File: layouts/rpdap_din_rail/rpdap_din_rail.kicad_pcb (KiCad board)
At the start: 2 copper layers, 95 x 50 mm, 67 parts

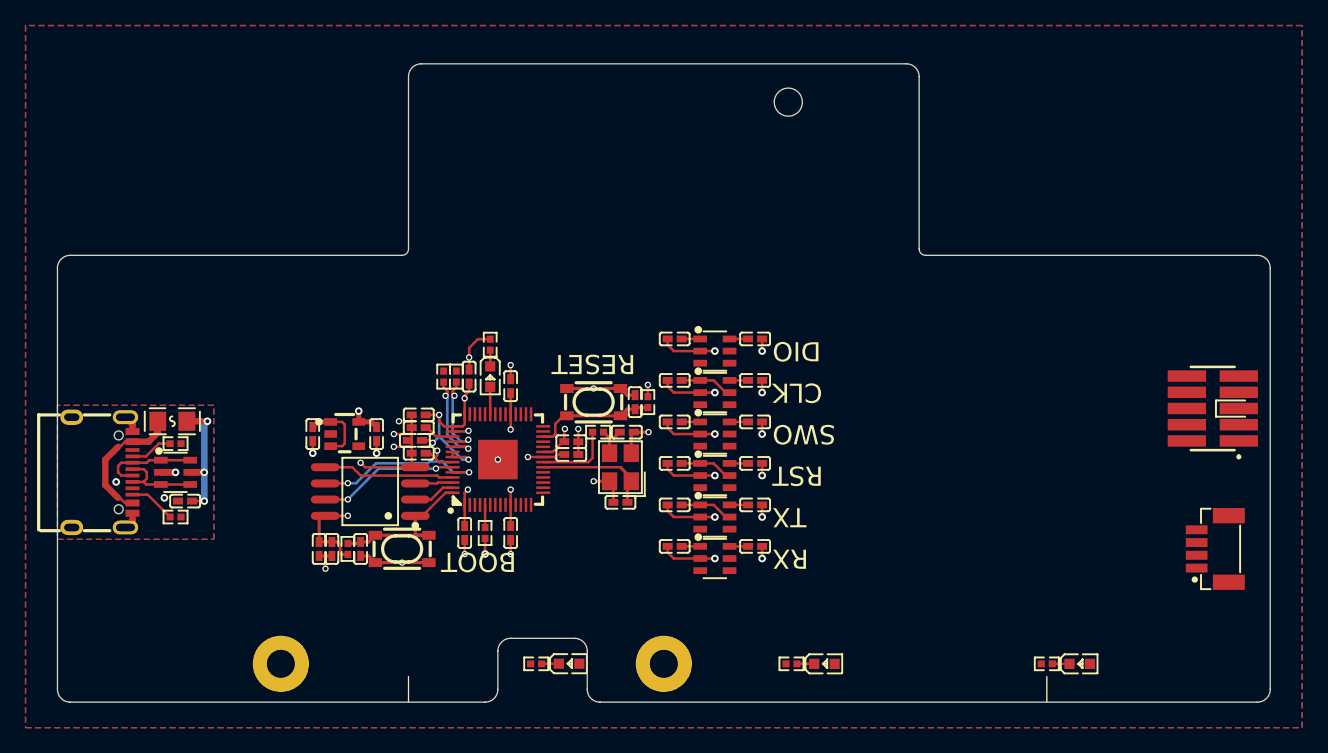
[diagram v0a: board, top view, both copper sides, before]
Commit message: update layouts and add jlink base compact layout
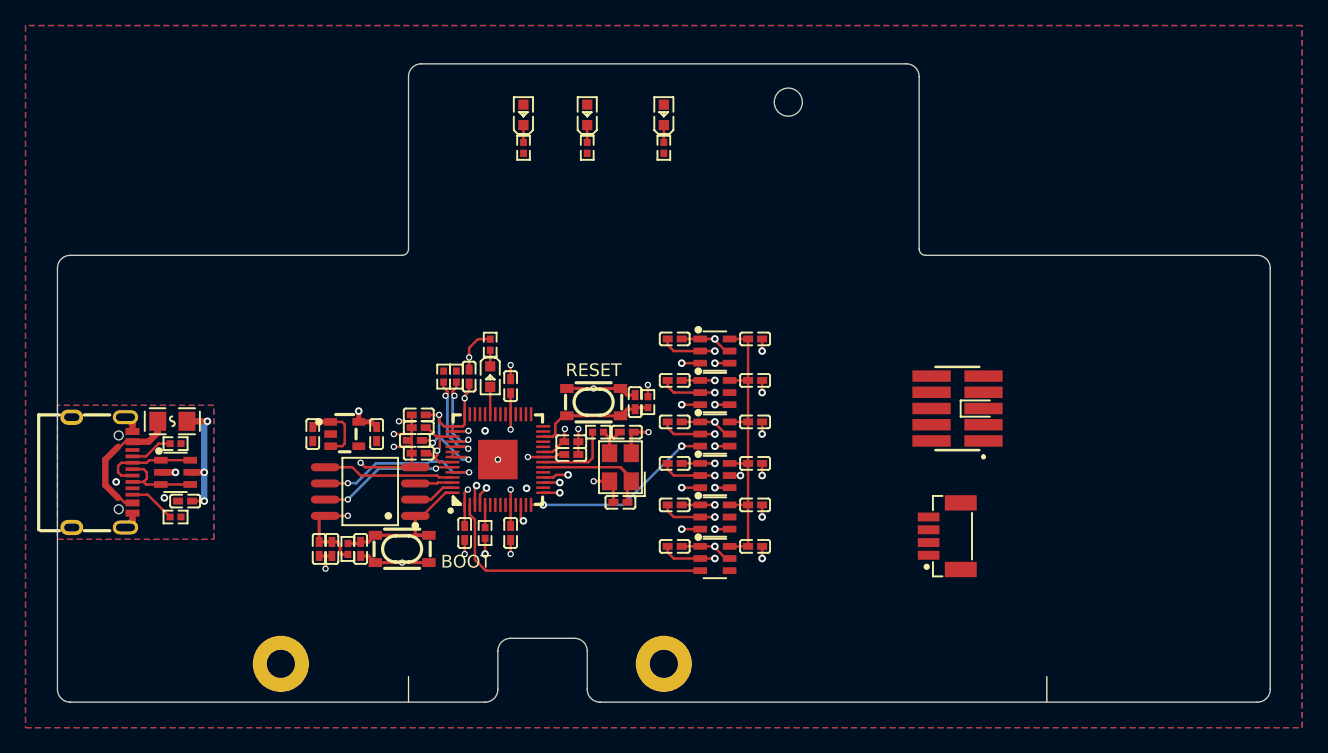
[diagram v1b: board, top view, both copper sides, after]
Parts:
- moved LED4 53.9 mm to (10.0, -43.0), turned to 90 degrees
- moved R12 50.3 mm to (10.0, -40.4), turned to -90 degrees
- moved LED3 46.8 mm to (4.00, -43.0), turned to 90 degrees
- moved R11 43.5 mm to (4.00, -40.4), turned to -90 degrees
- moved LED2 43.1 mm to (-1.00, -43.0), turned to 90 degrees
- moved R10 40.4 mm to (-0.99, -40.4), turned to -90 degrees
- moved U10 21.0 mm to (32.0, -10.0)
- moved CN1 20.0 mm to (33.0, -20.0)
- moved C10 9.75 mm to (17.2, -25.4)
- moved C3 9.75 mm to (10.8, -15.7)
- moved C4 9.75 mm to (17.2, -15.7)
- moved C9 9.75 mm to (10.8, -25.4)
- moved U2 9.75 mm to (14.0, -14.8)
- moved U5 9.75 mm to (14.0, -24.5)
- moved C11 3.25 mm to (10.8, -9.20)
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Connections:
- net -line renamed TARGET_SWCLK
- net GND_DETECT renamed TARGET_GND_DETECT
- net SWDIO renamed TARGET_SWDIO
- net SWO renamed TARGET_SWO
- net UART_RX renamed TARGET_UART_RX
- net UART_TX renamed TARGET_UART_TX
- net nRESET renamed TARGET_RESET
- U4 pad 5: (no net) -> GND
- U7 pad 5: (no net) -> GND
- U8 pad 19: TESTEN -> GND
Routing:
- net rpdap-line-5: track 0.00 -> 22.5 mm
- net rpdap-line-6: track 0.00 -> 21.8 mm, vias 0 -> 2
- net rpdap-line-1: track 0.00 -> 20.7 mm, vias 0 -> 2
- net -hv: track 8.70 -> 25.0 mm
- net rpdap-line-4: track 0.00 -> 16.0 mm, vias 0 -> 2
- net rpdap-line-3: track 0.00 -> 15.6 mm, vias 0 -> 2
- net rpdap-line-2: track 0.00 -> 15.2 mm, vias 0 -> 2
- net DVDD: track 8.41 -> 21.1 mm
- net rpdap-line-0: track 0.00 -> 12.5 mm, vias 0 -> 2
- net 3V3: track 57.2 -> 60.8 mm, vias 13 -> 19
- net anode-0: track 0.00 -> 2.15 mm
- net (no net): track 2.15 -> 0.00 mm
- net GND: track 78.2 -> 76.3 mm
- net anode-1: track 0.00 -> 1.53 mm, vias 0 -> 1
- net TARGET_UART_RX: track 0.00 -> 1.15 mm, vias 0 -> 1
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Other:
- copper layers 2 -> 4
- board text removed: "CLK"
- board text removed: "DIO"
- board text removed: "RST"
- board text removed: "RX"
- board text removed: "SWO"
- board text removed: "TX"
